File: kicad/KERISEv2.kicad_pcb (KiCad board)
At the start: 2 copper layers, 58 x 62 mm, 118 parts, among them P1 MT-ENC, P10 USB_A, P11 BAT1, P12 BAT2, P2 MT-ENC, P3 Battery_A, P4 Battery_B, P5 SWD, P6 UART, P7 USB_A, P8 BAT1, P9 BAT2, Q1 IRLML6402, Q2 IRFML8244, Q3 IRFML8244, Q4 BSS138, SW1 RESET, SW2 Power, SW3 BUTTON, U1 STM32F405RGTx, U10 MCP73831, U11 MCP73831, U12 MCP73831, U2 DRV8835, U3 DRV8835, U4 LXDC55FAAA-203, U5 REF1933, U6 LT1963ES8, U7 AD8604, U8 MPU6500, U9 MCP73831

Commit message: 新基板，部品を配置
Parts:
- removed G***: LOGO, KERI:KERI_25mm
- added D14: LED, LEDs:LED_0603, F.Cu at (147.5, 101.0)
- added D15: LED, LEDs:LED_0603, F.Cu at (150.5, 102.0)
- added R22: 1k, Resistors_SMD:R_0402, F.Cu at (149.0, 102.0)
- added R23: 1k, Resistors_SMD:R_0402, F.Cu at (150.0, 104.5)
- D2, D8: footprint mouse:LED-5MM_Angle -> mouse:LED-5MM_Angle_wide
- moved R2 59.1 mm to (160.5, 156.5), turned to 180 degrees
- moved D1 55.0 mm to (153.5, 156.5)
- moved P5 53.6 mm to (128.0, 155.0)
- moved R25 42.6 mm to (130.0, 173.0), turned to 0 degrees
- moved R30 42.6 mm to (156.0, 173.0), turned to 180 degrees
- moved P10 41.3 mm to (160.0, 167.0), turned to 270 degrees
- moved P7 41.3 mm to (126.0, 167.0), turned to 90 degrees
- moved D16 40.5 mm to (130.0, 170.0)
- moved D19 40.5 mm to (156.0, 170.0)
- moved R27 39.6 mm to (133.0, 172.0), turned to 0 degrees
- moved R32 39.6 mm to (153.0, 172.0), turned to 180 degrees
- moved U12 36.3 mm to (153.0, 169.0), turned to 0 degrees
- moved U9 36.3 mm to (133.0, 169.0), turned to 180 degrees
- moved C33 36.1 mm to (130.0, 167.0)
- moved C36 36.1 mm to (156.0, 167.0), turned to 270 degrees
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- renumbered D14 to D16, D15 to D17, D16 to D18, D17 to D19, R22 to R24, R23 to R25, R24 to R26, R25 to R27, R26 to R28, R27 to R29, R28 to R30, R29 to R31, R30 to R32
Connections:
- U1 pad 40: (no net) -> LED_5
- U1 pad 51: (no net) -> LED_6
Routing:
- net GND: track 1236.0 -> 0.00 mm, vias 536 -> 0
- net +3V3: track 153.0 -> 0.00 mm, vias 7 -> 0
- net +5V: track 141.6 -> 0.00 mm, vias 4 -> 0
- net +BATT: track 101.0 -> 0.00 mm, vias 1 -> 0
- net +3.3VADC: track 96.0 -> 0.00 mm, vias 4 -> 0
- net RESET: track 67.7 -> 0.00 mm, vias 5 -> 0
- net /Charger A/VSS: track 64.7 -> 0.00 mm
- net /Charger B/VSS: track 63.8 -> 0.00 mm
- net EN-R-A: track 57.7 -> 0.00 mm, vias 2 -> 0
- net EN-R-B: track 56.3 -> 0.00 mm, vias 1 -> 0
- net BUTTON: track 52.5 -> 0.00 mm, vias 2 -> 0
- net Net-(C22-Pad2): track 51.1 -> 0.00 mm, vias 2 -> 0
- net Net-(C24-Pad2): track 43.1 -> 0.00 mm, vias 4 -> 0
- net PR-RCV-FL: track 37.9 -> 0.00 mm, vias 2 -> 0
- net PR-RCV-SL: track 36.5 -> 0.00 mm, vias 2 -> 0
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- removed copper zone on B.Cu, net /Charger A/VSS
- removed copper zone on F.Cu, net /Charger A/VSS
- removed copper zone on B.Cu, net /Charger B/VSS
- removed copper zone on F.Cu, net /Charger B/VSS
- removed copper zone on B.Cu, net GND
- removed copper zone on F.Cu, net GND
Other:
- board size 58 x 62 mm -> 50 x 59 mm
- board text removed: "KERISE v2 2016.12.01"
- board text removed: "KERSE v2"

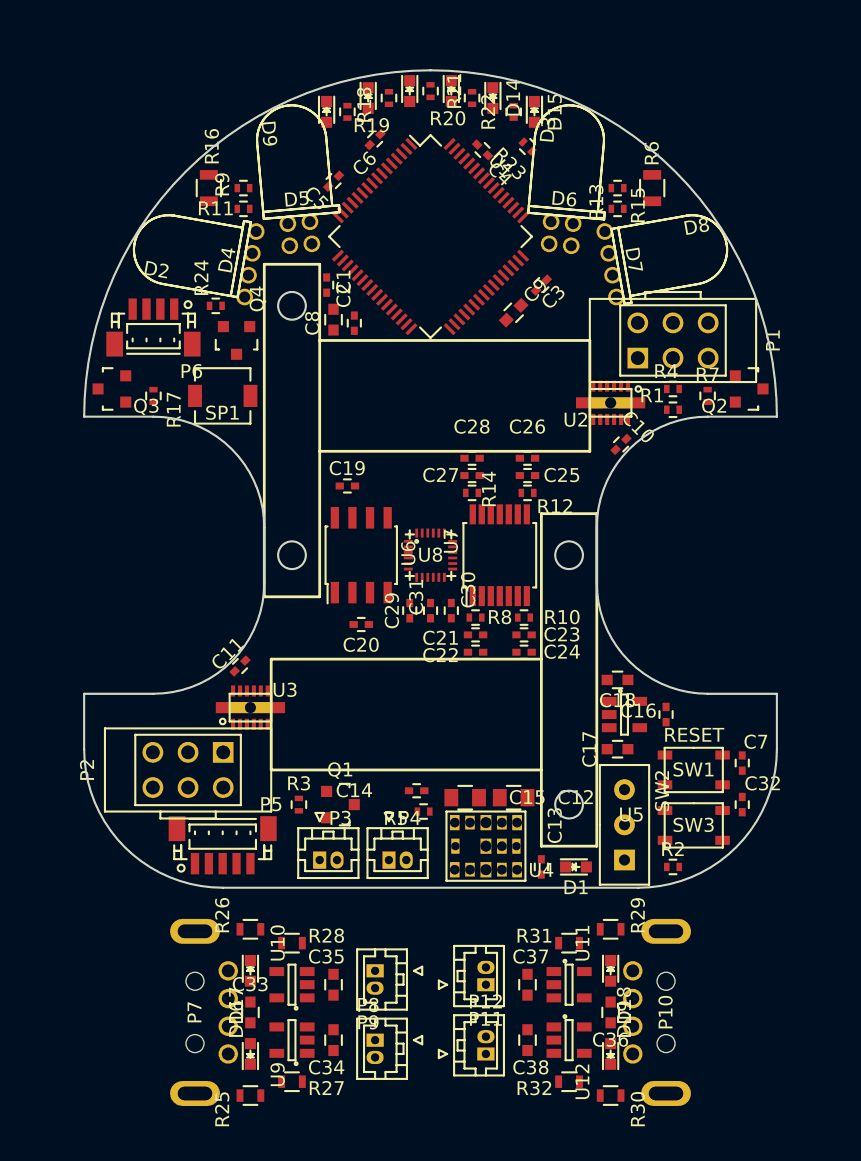
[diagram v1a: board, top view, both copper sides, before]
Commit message: 自動配線用にdsn吐き出し
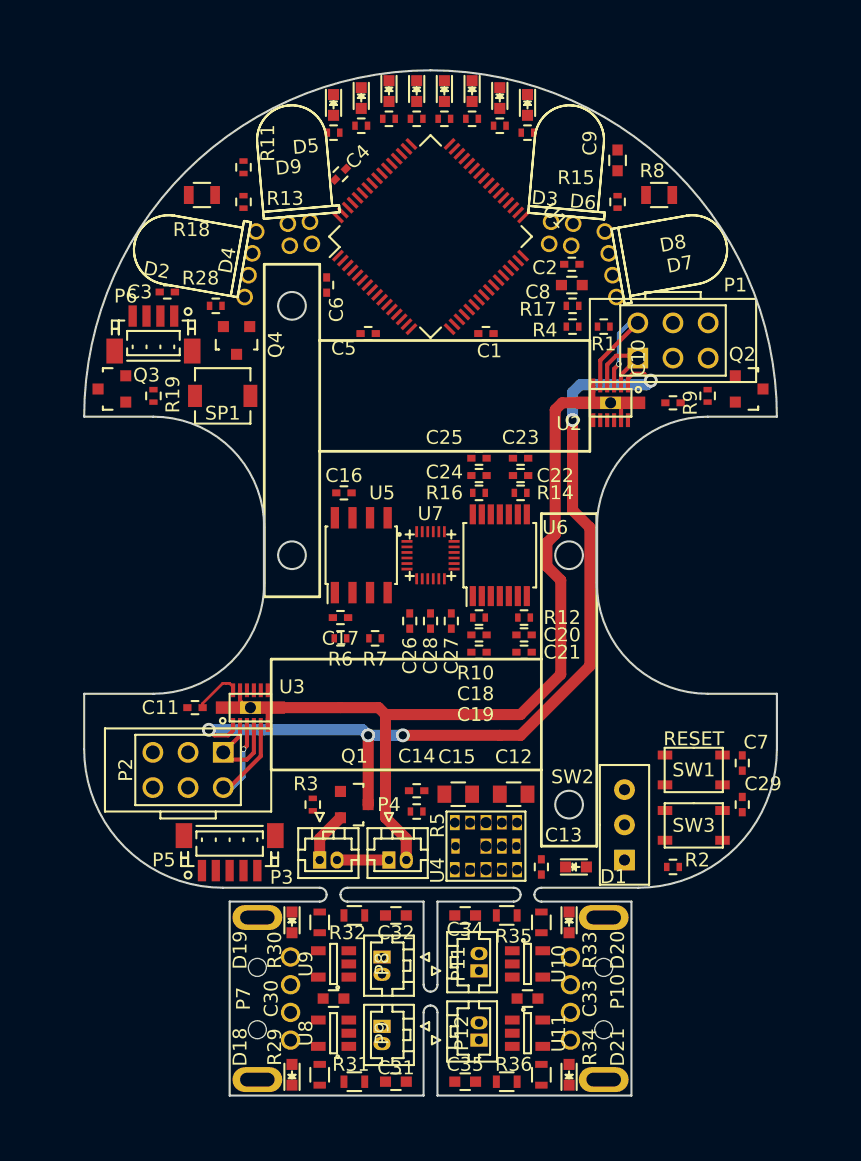
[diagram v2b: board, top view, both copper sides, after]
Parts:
- removed the C16 at (160.0, 145.5)
- removed the C17 at (156.5, 148.0)
- removed the C18 at (156.5, 143.0)
- removed the U5 at (157.0, 145.5)
- added D16: LED, LEDs:LED_0603, F.Cu at (138.0, 101.0)
- added D17: LED, LEDs:LED_0603, F.Cu at (136.0, 101.5)
- added G***: LOGO, KERI:KERI_22mm, B.Cu at (143.0, 128.0)
- added R26: 1k, Resistors_SMD:R_0402, F.Cu at (138.0, 103.0)
- added R27: 1k, Resistors_SMD:R_0402, F.Cu at (136.0, 103.5)
- added R6: 1k, Resistors_SMD:R_0402, F.Cu at (136.5, 140.0)
- added R7: 1k, Resistors_SMD:R_0402, F.Cu at (139.0, 140.0)
- moved C3 27.0 mm to (124.0, 115.0), turned to 180 degrees
- moved C8 17.4 mm to (153.2, 114.5), turned to 0 degrees
- moved C2 16.3 mm to (153.2, 113.0), turned to 0 degrees
- moved D10 14.5 mm to (150.0, 101.5)
- moved C9 13.3 mm to (156.5, 105.5), turned to 270 degrees
- moved R20 13.1 mm to (150.0, 103.5), turned to 180 degrees
- moved C1 12.0 mm to (147.0, 118.0), turned to 0 degrees
- moved C5 11.3 mm to (138.5, 118.0), turned to 180 degrees
- moved C6 11.1 mm to (135.5, 114.5), turned to 270 degrees
- moved D15 10.6 mm to (140.0, 100.5)
- moved C4 10.4 mm to (136.5, 106.5), turned to 45 degrees
- moved R25 10.2 mm to (140.0, 102.5), turned to 0 degrees
- moved D11 9.50 mm to (148.0, 101.0)
- moved R4 8.53 mm to (153.2, 117.5), turned to 180 degrees
- moved R21 8.25 mm to (148.0, 103.0), turned to 180 degrees
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- renumbered C19 to C16, C20 to C17, C21 to C18, C22 to C19, C23 to C20, C24 to C21, C25 to C22, C26 to C23, C27 to C24, C28 to C25, C29 to C26, C30 to C27, C31 to C28, C32 to C29, C33 to C30, C34 to C31, C35 to C32, C36 to C33, C37 to C34, C38 to C35, D16 to D18, D17 to D19, D18 to D20, D19 to D21, R8 to R10, R9 to R11, R10 to R12, R11 to R13, R12 to R14, R13 to R15, R14 to R16, R15 to R17, R16 to R18, R17 to R19, R18 to R20, R19 to R21, R20 to R22, R21 to R23, R22 to R24, R23 to R25, R24 to R28, R25 to R29, R26 to R30, R27 to R31, R28 to R32, R29 to R33, R30 to R34, R31 to R35, R32 to R36, R6 to R8, R7 to R9, U11 to U10, U12 to U11, U6 to U5, U7 to U6, U8 to U7, U9 to U8, U10 to U9
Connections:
- D4 pad 1: +3.3VADC -> +3V3
- D5 pad 1: +3.3VADC -> +3V3
- D6 pad 1: +3.3VADC -> +3V3
- D7 pad 1: +3.3VADC -> +3V3
- U1 pad 52: (no net) -> LED_7
- U1 pad 53: (no net) -> LED_8
- U1 pad 61: SPEAKER -> (no net)
- U1 pad 62: (no net) -> SPEAKER
- U6 pad 4: +3.3VADC -> +3V3
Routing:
- net GND: track 0.00 -> 68.3 mm
- net +BATT: track 0.00 -> 66.0 mm, vias 0 -> 5
- net /Motor_R/MT_OUT_2: track 0.00 -> 11.5 mm, vias 0 -> 1
- net /Motor_L/MT_OUT_2: track 0.00 -> 11.2 mm, vias 0 -> 1
- net /Motor_R/MT_OUT_1: track 0.00 -> 7.11 mm
- net /Motor_L/MT_OUT_1: track 0.00 -> 6.53 mm
- net /Power/BAT_to_BAT: track 0.00 -> 3.75 mm
- net /Power/BAT_to_FET: track 0.00 -> 3.67 mm
- net +3V3: track 0.00 -> 3.45 mm
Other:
- board size 50 x 59 mm -> 50 x 74 mm
- net class 3.3V: clearance 0.2 -> 0.1999; trace_width 0.2999 -> 0.2; via_dia 0.4 -> 0.36
- net class 5V: clearance 0.2 -> 0.1999; trace_width 0.4 -> 0.3; via_dia 0.5 -> 0.4
- net class AXIS: clearance 0.2 -> 0.1999; trace_width 0.1999 -> 0.2
- net class Charge: clearance 0.2 -> 0.1999; trace_width 0.3999 -> 0.3; via_dia 0.5 -> 0.4
- net class Default: clearance 0.2 -> 0.1999; trace_width 0.1999 -> 0.2
- net class GND: clearance 0.2 -> 0.1999; trace_width 0.4 -> 0.2; via_dia 0.5 -> 0.4
- net class IR_LED: clearance 0.2 -> 0.1999; trace_width 0.4 -> 0.3; via_dia 0.5 -> 0.4
- net class Motor: clearance 0.2 -> 0.1999; trace_width 0.8 -> 0.3; via_dia 1 -> 0.4; via_drill 0.6 -> 0.3
- net class VBAT: clearance 0.2 -> 0.1999; trace_width 0.8 -> 0.3; via_dia 1 -> 0.4; via_drill 0.6 -> 0.3
- rule trace_clearance: 0.2 -> 0.1999
- board text added: "2 x 1S 200mA"
- board text added: "KERISE v2 2016.12.28"

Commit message: 製造ファイル出力
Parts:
- moved C17 1.50 mm to (138.0, 138.5)
- moved C11 0.50 mm to (125.5, 145.0)
- moved R7 0.50 mm to (139.5, 140.0), turned to 0 degrees
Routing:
- net GND: track 68.3 -> 851.3 mm, vias 0 -> 280
- net +3V3: track 3.45 -> 179.8 mm, vias 0 -> 10
- net +5V: track 0.00 -> 124.7 mm, vias 0 -> 5
- net SWDIO: track 0.00 -> 94.2 mm, vias 0 -> 4
- net RESET: track 0.00 -> 82.1 mm, vias 0 -> 3
- net SWCLK: track 0.00 -> 65.0 mm, vias 0 -> 2
- net SWO: track 0.00 -> 62.3 mm, vias 0 -> 4
- net EN-R-A: track 0.00 -> 53.5 mm, vias 0 -> 1
- net Net-(C19-Pad2): track 0.00 -> 51.5 mm, vias 0 -> 2
- net /Charger A/VSS: track 0.00 -> 51.1 mm
- net EN-R-B: track 0.00 -> 50.4 mm, vias 0 -> 1
- net Net-(C23-Pad2): track 0.00 -> 49.5 mm, vias 0 -> 2
- net MT-IN-R-1: track 0.00 -> 48.8 mm, vias 0 -> 3
- net MT-IN-R-2: track 0.00 -> 48.5 mm, vias 0 -> 2
- net /Charger B/VSS: track 0.00 -> 48.5 mm, vias 0 -> 1
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- added copper zone on B.Cu, net /Charger A/VSS
- added copper zone on F.Cu, net /Charger A/VSS
- added copper zone on B.Cu, net /Charger B/VSS
- added copper zone on F.Cu, net /Charger B/VSS
- added copper zone on B.Cu, net GND
- added copper zone on F.Cu, net GND
